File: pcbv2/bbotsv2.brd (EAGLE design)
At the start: 70 x 60 mm, 14 parts

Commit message: connected everything to amica, not tested
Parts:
- removed BAT: (no value), adafruit:JST-PH-2-THM
- removed LED2: WS2812B, LEDWS2812:WS2812B
- added ALIMENTACION_11.1V: (no value), adafruit:JST-PH-2-THM
- added RES1, RES2: (no value), my-library:M0805
- added U$5: BB-USBTTL, my-library:1X05
- LED1: value WS2812B -> (none); device LEDWS2812:WS2812B -> my-library:M0805
- U$3: value ESP8266 -> ESP07-16PIN; device esp8266modules:ESP03 -> esp8266modules:ESP07-16PIN
- moved U$3 74.9 mm to (-36.8, 12.7), flipped to the top, turned to 0 degrees
- moved LED1 30.6 mm to (5.08, 3.81)
- moved D2-GPIO4 13.3 mm to (63.5, 19.1), turned to 0 degrees
- moved ARMA 8.89 mm to (57.1, 49.5)
- moved MOT_A 8.89 mm to (57.1, 34.3)
- moved MOT_B 8.89 mm to (57.1, 41.9)
- moved D1-GPIO5 8.89 mm to (63.5, 15.2), turned to 0 degrees
- moved U$1 8.89 mm to (8.89, 52.1)
- moved U$2 8.89 mm to (34.3, 41.9)
- moved U$4 6.48 mm to (21.6, 7.62)
- moved A0 6.35 mm to (63.5, 11.4), turned to 0 degrees
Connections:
- net N$3 renamed 12V
- new net 5V: A0.2, D1-GPIO5.2, D2-GPIO4.2, LED1.1, NODE1.VIN, U$4.OUT+
- new net N$17: NODE1.3V3@1, U$2.STBY, U$2.VCC
- new net N$18: D1-GPIO5.3, NODE1.D3
- new net N$3: LED1.2, RES1.2
- net 3V3: now also NODE1.3V3@2; no longer NODE1.3V3@1
- net N$1: now also ALIMENTACION_11.1V.2; no longer BAT.2
- net N$10: now also NODE1.D1; no longer NODE1.D4
- net N$12: now also D2-GPIO4.3, NODE1.D4; no longer NODE1.D3, U$2.PWMB
- net N$19: now also U$3.TX, U$5.RX; no longer D2-GPIO4.3, NODE1.D2
- net N$2: now also ALIMENTACION_11.1V.1; no longer BAT.1
- net N$20: now also U$3.RX, U$5.TX; no longer D1-GPIO5.3, NODE1.D1
- net N$4: now also NODE1.D8; no longer NODE1.D7
- net N$5: now also NODE1.D7, U$2.PWMB; no longer A0.2, D1-GPIO5.2, D2-GPIO4.2, NODE1.VIN, U$2.STBY, U$2.VCC, U$4.OUT+
- net N$6: now also RES1.1, U$3.GND, U$5.GND
- net N$9: now also NODE1.D2; no longer NODE1.3V3@2

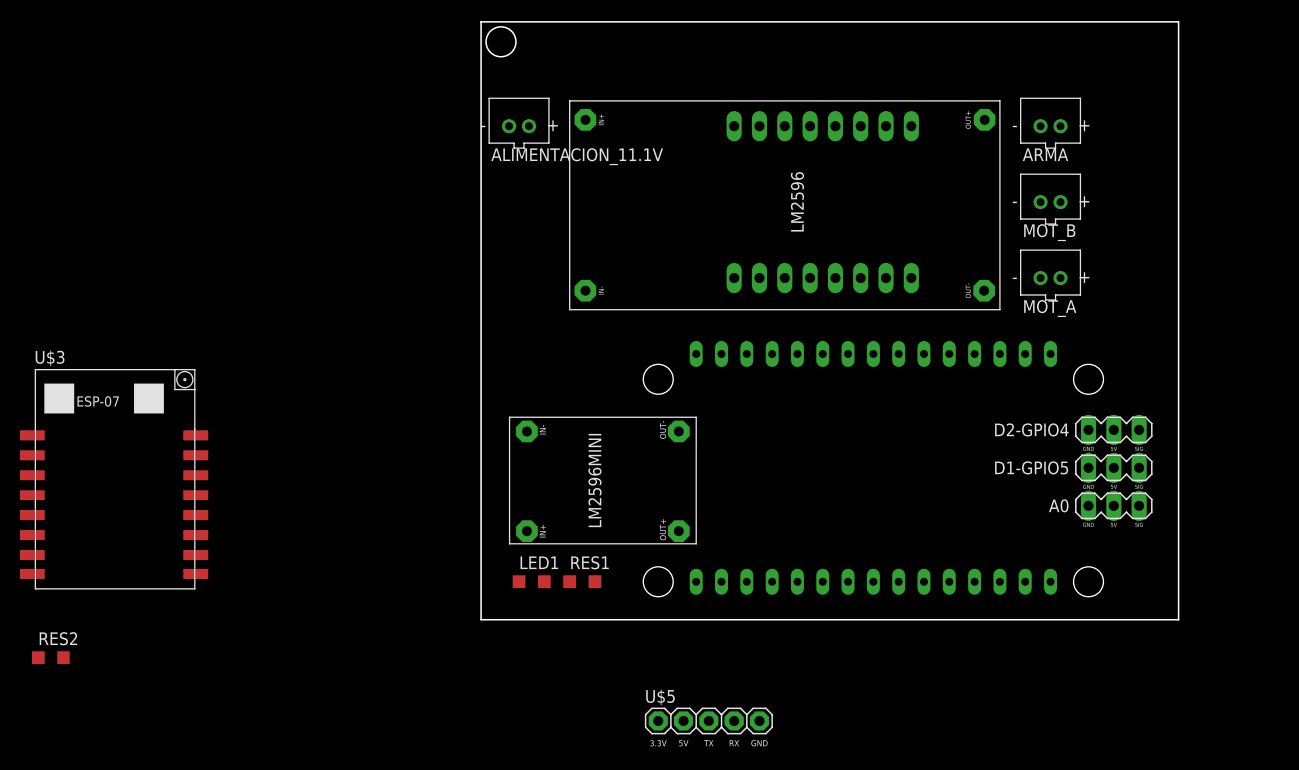
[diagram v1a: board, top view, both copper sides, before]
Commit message: connected esp07 on schematic and ruted all components
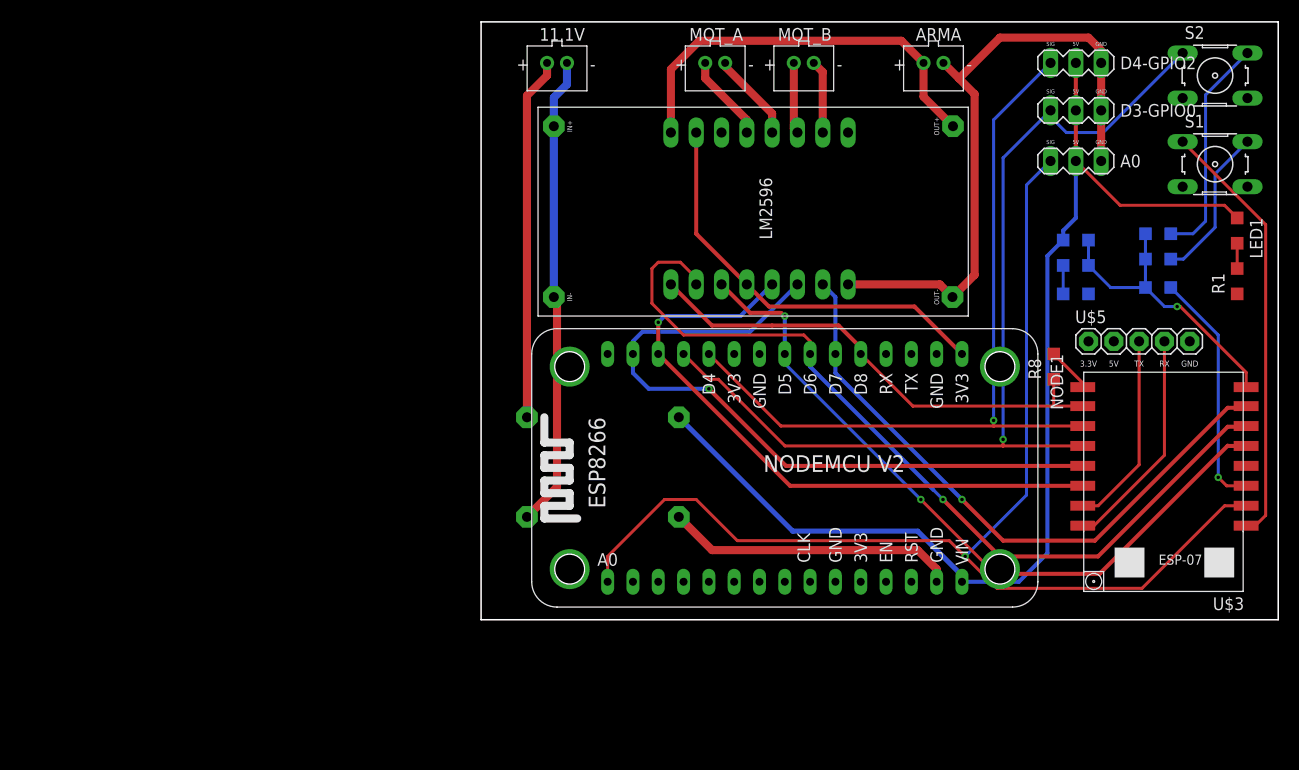
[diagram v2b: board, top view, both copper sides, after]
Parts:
- removed ALIMENTACION_11.1V: (no value), adafruit:JST-PH-2-THM
- removed D1-GPIO5, D2-GPIO4: BB-PIN3, my-library:BB-PIN3
- removed RES1, RES2: (no value), my-library:M0805
- added 11.1V: (no value), adafruit:JST-PH-2-THM
- added D3-GPIO0, D4-GPIO2: BB-PIN3, my-library:BB-PIN3
- added R1: 1k, my-library:M0805
- added R2, R3, R4, R5, R6, R7, R8: 10k, my-library:M0805
- added S1, S2: (no value), switch-omron:B3F-10XX
- moved U$3 105.4 mm to (68.6, 15.2), turned to 180 degrees
- moved LED1 79.1 mm to (75.9, 39.1), turned to 270 degrees
- moved U$5 57.6 mm to (66.0, 27.9)
- moved MOT_A 40.0 mm to (23.5, 55.9), turned to 180 degrees
- moved A0 34.8 mm to (59.7, 46.0), turned to 180 degrees
- moved MOT_B 28.4 mm to (32.4, 55.9), turned to 180 degrees
- moved U$4 14.0 mm to (21.6, 21.6), flipped to the bottom, turned to 270 degrees
- moved ARMA 13.4 mm to (45.4, 55.9), turned to 180 degrees
- moved NODE1 11.4 mm to (29.2, 15.2), flipped to the top
- moved U$2 6.38 mm to (27.9, 41.3)
- moved U$1 3.24 mm to (5.71, 51.4)
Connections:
- removed net N$11: A0.1, ARMA.1, D1-GPIO5.1, D2-GPIO4.1, U$1.OUT-, U$2.GND
- removed net N$2: ALIMENTACION_11.1V.1, U$1.IN-, U$4.IN+
- removed net N$6: NODE1.GND@4, RES1.1, U$3.GND, U$4.OUT-, U$5.GND
- new net 3.3: R2.1, R3.1, R4.1, R5.2, R7.2, U$3.VCC
- new net GND2: 11.1V.2, A0.1, ARMA.2, D3-GPIO0.1, D4-GPIO2.1, NODE1.GND@4, R1.1, R6.1, R8.2, S1.3, S1.4, S2.3, S2.4, U$1.IN-, U$1.OUT-, U$2.GND, U$2.GND3, U$3.GND, U$4.IN-, U$4.OUT-, U$5.GND
- new net N$22: R2.2, S1.2
- new net N$23: R3.2, S2.2
- new net N$25: R5.1, R6.2
- new net N$27: S1.1, U$3.REST
- new net N$28: R7.1, U$3.CH_PD
- net 12V: now also ARMA.1; no longer ARMA.2
- net 5V: now also D3-GPIO0.2, D4-GPIO2.2, R4.2; no longer D1-GPIO5.2, D2-GPIO4.2
- net N$1: now also 11.1V.1, U$4.IN+; no longer ALIMENTACION_11.1V.2, U$4.IN-
- net N$10: now also U$3.GPIO5
- net N$12: now also D4-GPIO2.3, U$3.GPIO2; no longer D2-GPIO4.3
- net N$13: now also MOT_A.2; no longer MOT_A.1
- net N$14: now also MOT_A.1; no longer MOT_A.2
- net N$15: now also MOT_B.1; no longer MOT_B.2
- net N$16: now also MOT_B.2; no longer MOT_B.1
- net N$18: now also D3-GPIO0.3, S2.1, U$3.GPIO0; no longer D1-GPIO5.3
- net N$21: now also U$3.ADC
- net N$3: now also R1.2; no longer RES1.2
- net N$4: now also R8.1, U$3.GPIO15
- net N$5: now also U$3.GPIO13
- net N$7: now also U$3.GPIO12
- net N$8: now also U$3.GPIO14
- net N$9: now also U$3.GPIO4
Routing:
- net GND2: track 0.00 -> 146.0 mm
- net N$21: track 0.00 -> 119.4 mm, vias 0 -> 1
- net 5V: track 0.00 -> 114.3 mm
- net N$18: track 0.00 -> 97.4 mm, vias 0 -> 1
- net N$7: track 0.00 -> 86.6 mm, vias 0 -> 1
- net N$12: track 0.00 -> 79.3 mm, vias 0 -> 1
- net N$8: track 0.00 -> 73.0 mm, vias 0 -> 2
- net N$10: track 0.00 -> 71.1 mm, vias 0 -> 1
- net N$9: track 0.00 -> 64.3 mm, vias 0 -> 1
- net N$5: track 0.00 -> 63.2 mm, vias 0 -> 1
- net N$4: track 0.00 -> 49.5 mm
- net N$27: track 0.00 -> 43.3 mm
- net N$17: track 0.00 -> 41.8 mm
- net 12V: track 0.00 -> 41.4 mm
- net N$1: track 0.00 -> 36.4 mm
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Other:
- board size 70 x 60 mm -> 80 x 60 mm

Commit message: changed version of lm2596mini
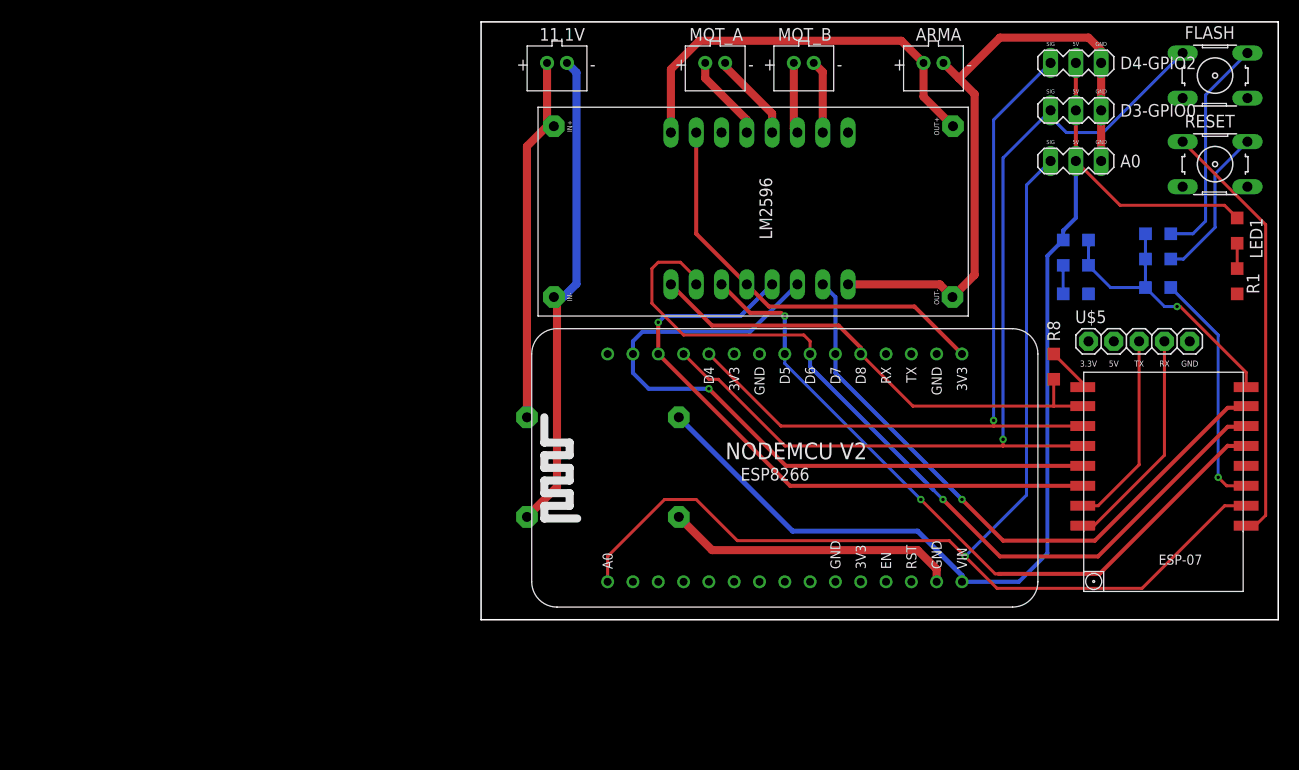
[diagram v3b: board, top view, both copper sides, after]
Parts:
- renumbered S1 to RESET, S2 to FLASH
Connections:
- net N$1 renamed 11.1
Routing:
- net GND2: track 146.0 -> 147.3 mm
- net 11.1: track 36.4 -> 37.1 mm
